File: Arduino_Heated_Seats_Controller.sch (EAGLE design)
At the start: 21 parts, among them U1 MEGA8-AI, U2 UA78M05CDCY, U3 ULN2003ADE4, U4 IC_TD62783-SO-18W

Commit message: Library error - need to make sure the rest of my libraries are correct are well.
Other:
- moved on the sheet: U4

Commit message: More patching.
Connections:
- net VIN: now also U3.COM
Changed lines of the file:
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@@
 <instance part="SUPPLY16" gate="GND" x="116.84" y="99.06"/>
 <instance part="SUPPLY12" gate="GND" x="154.94" y="109.22"/>
-<instance part="SUPPLY17" gate="GND" x="132.08" y="63.754"/>
+<instance part="SUPPLY17" gate="GND" x="129.54" y="63.754"/>
 <instance part="R1" gate="G$1" x="157.48" y="132.08"/>
 <instance part="R2" gate="G$1" x="167.64" y="134.62"/>
@@
 <segment>
 <pinref part="SUPPLY17" gate="GND" pin="GND"/>
-<wire x1="132.08" y1="66.294" x2="132.08" y2="68.58" width="0.1524" layer="91"/>
+<wire x1="129.54" y1="66.294" x2="129.54" y2="66.04" width="0.1524" layer="91"/>
 <pinref part="U3" gate="A" pin="E"/>
-<wire x1="139.7" y1="71.12" x2="132.08" y2="71.12" width="0.1524" layer="91"/>
-<wire x1="132.08" y1="68.58" x2="132.08" y2="71.12" width="0.1524" layer="91"/>
+<wire x1="139.7" y1="71.12" x2="129.54" y2="71.12" width="0.1524" layer="91"/>
+<wire x1="129.54" y1="66.04" x2="129.54" y2="71.12" width="0.1524" layer="91"/>
 </segment>
 </net>
@@
 <junction x="33.02" y="139.7"/>
 </segment>
+<segment>
+<pinref part="U3" gate="A" pin="COM"/>
+<wire x1="137.16" y1="68.58" x2="139.7" y2="68.58" width="0.1524" layer="91"/>
+<wire x1="137.16" y1="68.58" x2="135.89" y2="68.58" width="0.1524" layer="91"/>
+<label x="135.89" y="68.58" size="1.27" layer="95" rot="R180" xref="yes"/>
+</segment>
 </net>

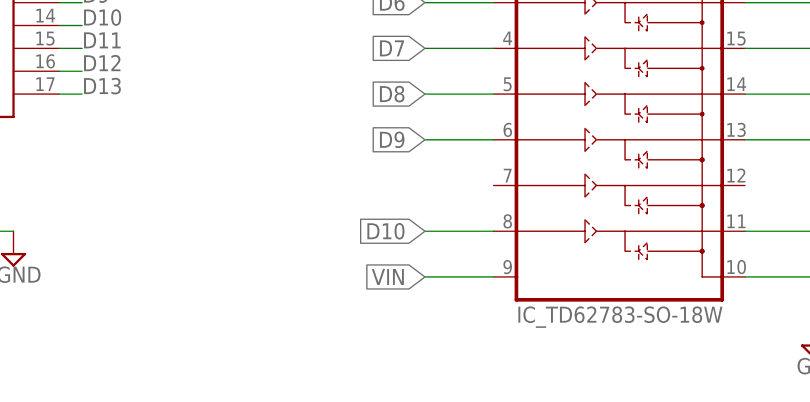
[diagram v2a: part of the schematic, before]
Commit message: Grounding unused input pins (compatibility with A2982SLWTR-T). Tweak routing and vias.
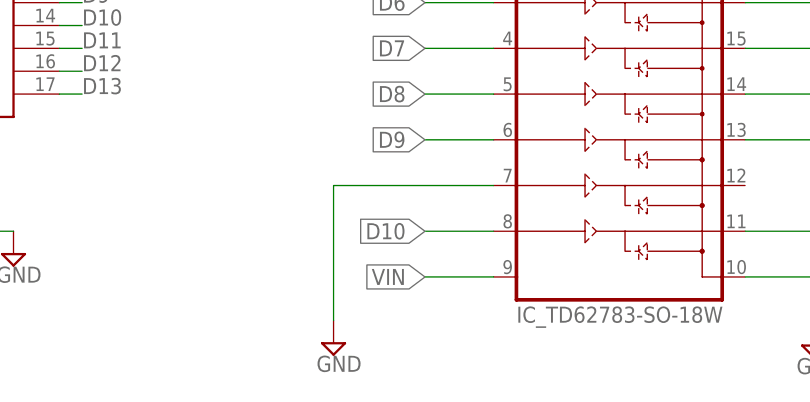
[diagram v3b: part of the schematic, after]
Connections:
- net GND: now also U4.IN7
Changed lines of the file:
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@@
 <part name="SUPPLY9" library="supply2" deviceset="GND" device=""/>
 <part name="C2" library="rcl" deviceset="C-US" device="C0603" value="0.1uF"/>
+<part name="SUPPLY13" library="supply2" deviceset="GND" device=""/>
 </parts>
 <sheets>
@@
 <instance part="SUPPLY9" gate="GND" x="78.74" y="104.14"/>
 <instance part="C2" gate="G$1" x="27.94" y="119.38"/>
+<instance part="SUPPLY13" gate="GND" x="124.46" y="2.794"/>
 </instances>
 <busses>
@@
 <wire x1="129.54" y1="66.04" x2="129.54" y2="71.12" width="0.1524" layer="91"/>
 </segment>
+<segment>
+<pinref part="U4" gate="IC" pin="IN7"/>
+<wire x1="142.24" y1="20.32" x2="124.46" y2="20.32" width="0.1524" layer="91"/>
+<wire x1="124.46" y1="20.32" x2="124.46" y2="5.334" width="0.1524" layer="91"/>
+<pinref part="SUPPLY13" gate="GND" pin="GND"/>
+</segment>
 </net>

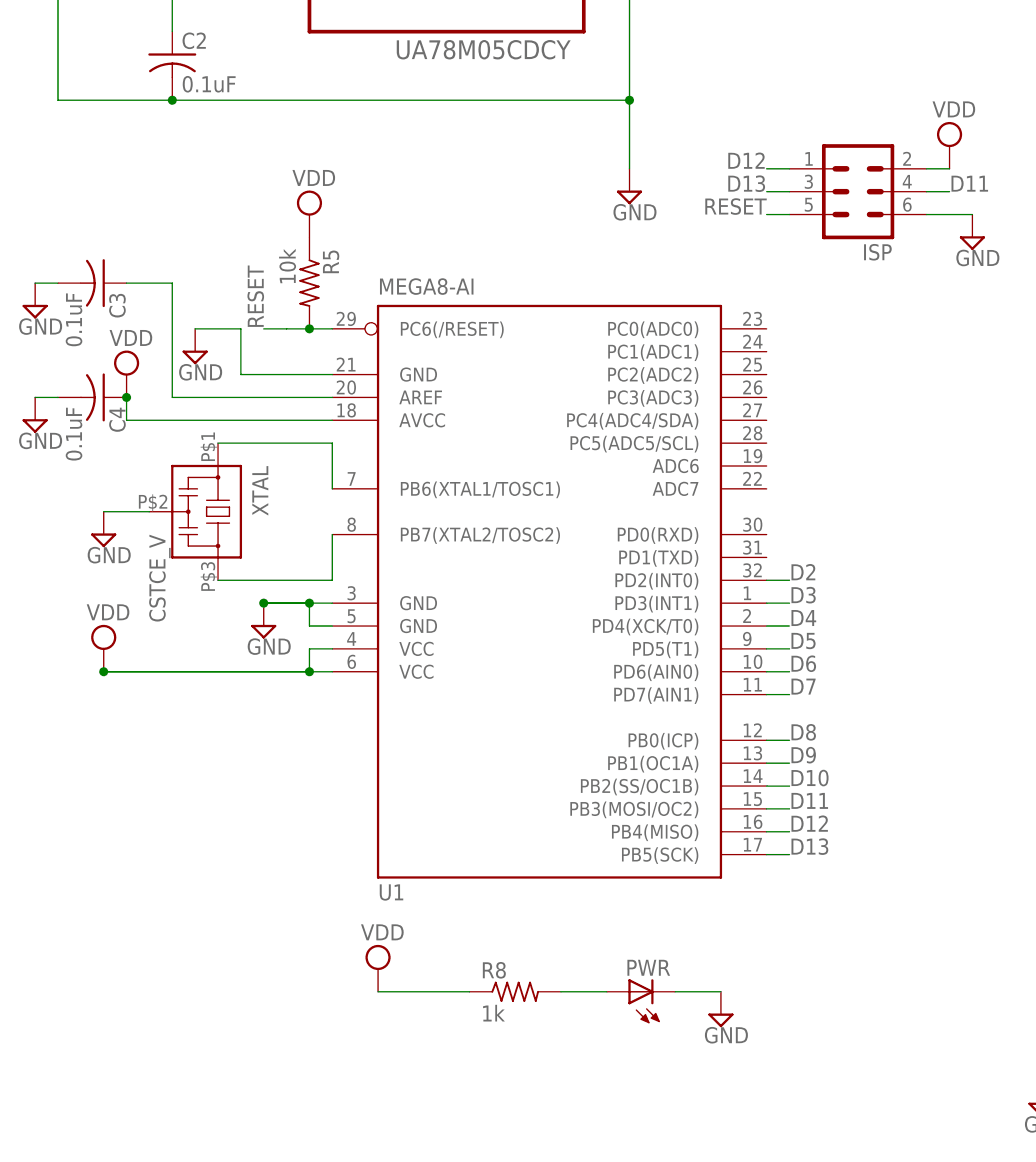
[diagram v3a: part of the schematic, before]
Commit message: Swapped ATMega from unknown library with Element14 library. Moved silkscreen (web address) to other side of board.
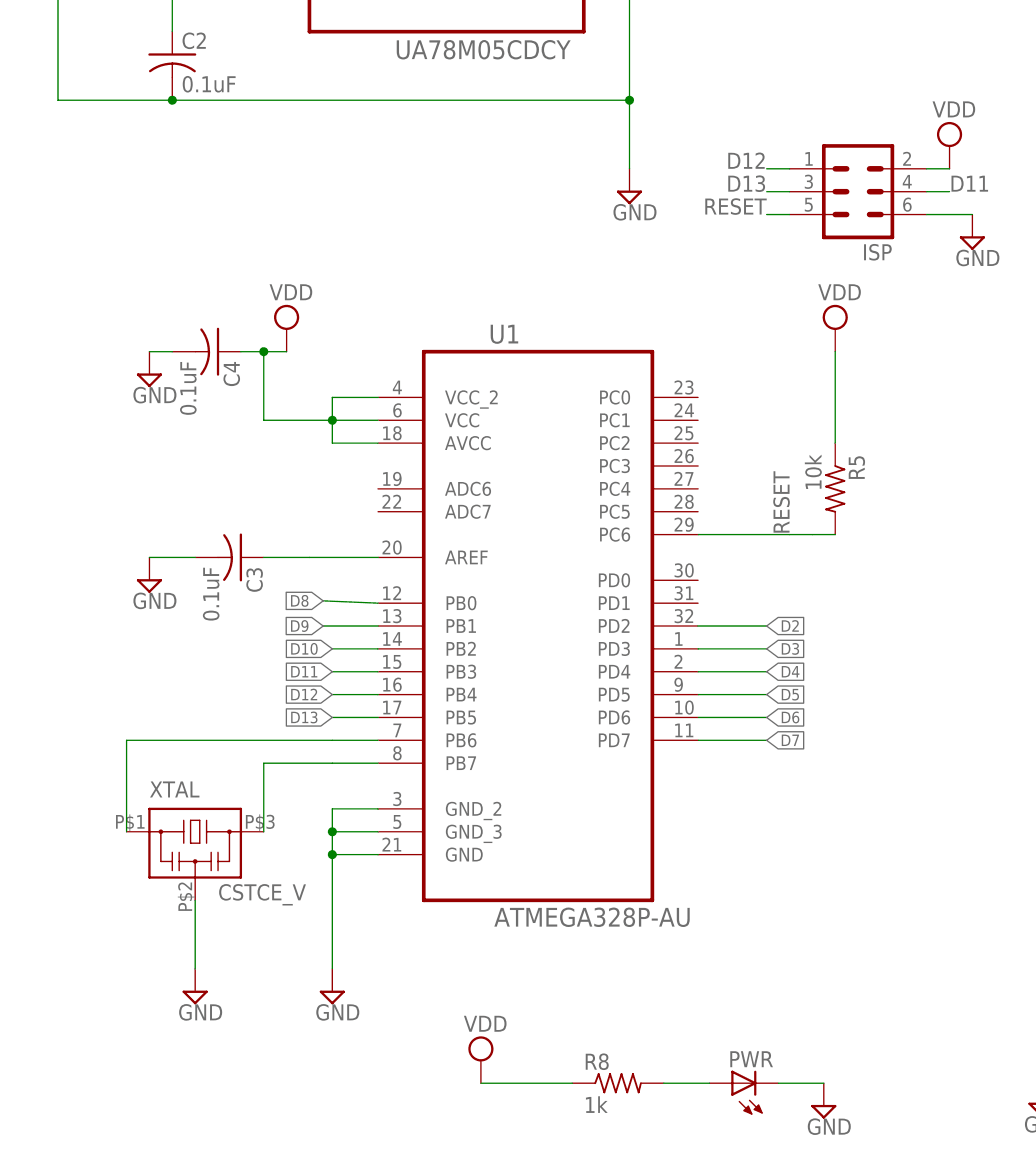
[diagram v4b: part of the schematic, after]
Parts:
- U1: value MEGA8-AI -> ATMEGA328P-AU; device atmel:MEGA8-AI -> Atmel_By_element14_Batch_1-00:ATMEGA328P-AU
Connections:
- net D10: now also U1.PB2; no longer U1.PB2(SS/OC1B)
- net D11: now also U1.PB3; no longer U1.PB3(MOSI/OC2)
- net D12: now also U1.PB4; no longer U1.PB4(MISO)
- net D13: now also U1.PB5; no longer U1.PB5(SCK)
- net D2: now also U1.PD2; no longer U1.PD2(INT0)
- net D3: now also U1.PD3; no longer U1.PD3(INT1)
- net D4: now also U1.PD4; no longer U1.PD4(XCK/T0)
- net D5: now also U1.PD5; no longer U1.PD5(T1)
- net D6: now also U1.PD6; no longer U1.PD6(AIN0)
- net D7: now also U1.PD7; no longer U1.PD7(AIN1)
- net D8: now also U1.PB0; no longer U1.PB0(ICP)
- net D9: now also U1.PB1; no longer U1.PB1(OC1A)
- net GND: now also U1.GND_2, U1.GND_3; no longer U1.GND@1, U1.GND@2
- net PB6: now also U1.PB6; no longer U1.PB6(XTAL1/TOSC1)
- net PB7: now also U1.PB7; no longer U1.PB7(XTAL2/TOSC2)
- net RESET: now also U1.PC6; no longer U1.PC6(/RESET)
- net VDD: now also U1.VCC, U1.VCC_2; no longer U1.VCC@1, U1.VCC@2
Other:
- moved on the sheet: C3, C4, PWR, R5, R8, XTAL

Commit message: Enough changes to warrant a minor revision bump. Equivalent parts have been selected for testing - will need to update design if tests are good. Current design should be compatible with selected parts (will order parts before sending to fab house).
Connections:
- net D-BTN: now also BTN-IN.2, R2.1; no longer BTN-IN.1, R1.1
- net D2: now also R2.2, R4.1; no longer R1.2, R3.1
- net D3: now also R1.2, R3.1; no longer R2.2, R4.1
- net P-BTN: now also BTN-IN.1, R1.1; no longer BTN-IN.2, R2.1
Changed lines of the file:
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@@
 <net name="D2" class="0">
+<segment>
+<pinref part="U1" gate="A" pin="PD2"/>
+<wire x1="86.36" y1="55.88" x2="93.98" y2="55.88" width="0.1524" layer="91"/>
+<label x="93.98" y="55.88" size="1.27" layer="95" xref="yes"/>
+</segment>
+<segment>
+<wire x1="180.34" y1="121.92" x2="180.34" y2="134.62" width="0.1524" layer="91"/>
+<wire x1="180.34" y1="134.62" x2="172.72" y2="134.62" width="0.1524" layer="91"/>
+<wire x1="180.34" y1="134.62" x2="187.96" y2="134.62" width="0.1524" layer="91"/>
+<junction x="180.34" y="134.62"/>
+<label x="187.96" y="134.62" size="1.27" layer="95" xref="yes"/>
+<pinref part="R2" gate="G$1" pin="2"/>
+<pinref part="R4" gate="G$1" pin="1"/>
+</segment>
+</net>
+<net name="D3" class="0">
+<segment>
+<pinref part="U1" gate="A" pin="PD3"/>
+<wire x1="86.36" y1="53.34" x2="93.98" y2="53.34" width="0.1524" layer="91"/>
+<label x="93.98" y="53.34" size="1.27" layer="95" xref="yes"/>
+</segment>
 <segment>
 <wire x1="175.26" y1="129.54" x2="175.26" y2="132.08" width="0.1524" layer="91"/>
@@
 <pinref part="R3" gate="G$1" pin="1"/>
 </segment>
-<segment>
-<pinref part="U1" gate="A" pin="PD2"/>
-<wire x1="86.36" y1="55.88" x2="93.98" y2="55.88" width="0.1524" layer="91"/>
-<label x="93.98" y="55.88" size="1.27" layer="95" xref="yes"/>
-</segment>
-</net>
-<net name="D3" class="0">
-<segment>
-<wire x1="180.34" y1="121.92" x2="180.34" y2="134.62" width="0.1524" layer="91"/>
-<wire x1="180.34" y1="134.62" x2="172.72" y2="134.62" width="0.1524" layer="91"/>
-<wire x1="180.34" y1="134.62" x2="187.96" y2="134.62" width="0.1524" layer="91"/>
-<junction x="180.34" y="134.62"/>
-<label x="187.96" y="134.62" size="1.27" layer="95" xref="yes"/>
-<pinref part="R2" gate="G$1" pin="2"/>
-<pinref part="R4" gate="G$1" pin="1"/>
-</segment>
-<segment>
-<pinref part="U1" gate="A" pin="PD3"/>
-<wire x1="86.36" y1="53.34" x2="93.98" y2="53.34" width="0.1524" layer="91"/>
-<label x="93.98" y="53.34" size="1.27" layer="95" xref="yes"/>
-</segment>
 </net>
 <net name="D-BTN" class="0">
-<segment>
-<wire x1="152.4" y1="132.08" x2="139.7" y2="132.08" width="0.1524" layer="91"/>
-<pinref part="BTN-IN" gate="G$1" pin="1"/>
-<label x="144.78" y="132.08" size="1.27" layer="95" rot="R270" xref="yes"/>
-<pinref part="R1" gate="G$1" pin="1"/>
-</segment>
-</net>
-<net name="P-BTN" class="0">
 <segment>
 <pinref part="BTN-IN" gate="G$1" pin="2"/>
@@
 </segment>
 </net>
+<net name="P-BTN" class="0">
+<segment>
+<wire x1="152.4" y1="132.08" x2="139.7" y2="132.08" width="0.1524" layer="91"/>
+<pinref part="BTN-IN" gate="G$1" pin="1"/>
+<label x="144.78" y="132.08" size="1.27" layer="95" rot="R270" xref="yes"/>
+<pinref part="R1" gate="G$1" pin="1"/>
+</segment>
+</net>

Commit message: Changes from freelancer.com - lovely~
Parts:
- removed PWR: (no value), led:LEDCHIP-LED0603
- removed R8: 1k, resistor:R-US_R0603
- added L, ON: (no value), led:LEDCHIP-LED0603
- added R6, R7: 1K, resistor:R-US_R0603
- R1, R2: value 15k -> 15K
- R3, R4, R5: value 10k -> 10K
- U2: value UA78M05CDCY -> UA78M05; device Texas Instruments_By_element14_Batch_1:UA78M05CDCY -> Roylib Regulator:UA78M05
- U3: value ULN2003ADE4 -> TPL7407L; device Texas Instruments_By_element14_Batch_1:ULN2003ADE4 -> Roylib Drivers:TPL7407L
- U4: value IC_TD62783-SO-18W -> A2982; device dp_devices:IC_TD62783-SO-18W -> Roylib Drivers:A2982
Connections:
- new net N$1: L.A, R6.2
- net D13: now also R6.1
- net D4: now also U3.IN7; no longer U3.7B
- net D5: now also U3.IN6; no longer U3.6B
- net D6: now also U3.IN5; no longer U3.5B
- net D7: now also U3.IN3; no longer U3.3B
- net D8: now also U3.IN2; no longer U3.2B
- net D9: now also U3.IN1; no longer U3.1B
- net DL-HIGH: now also U3.!OUT7; no longer U3.7C
- net DL-LOW: now also U3.!OUT5; no longer U3.5C
- net DL-MID: now also U3.!OUT6; no longer U3.6C
- net GND: now also L.C, ON.C, U2.GND, U3.GND; no longer PWR.C, U2.COMMON, U2.COMMON_2, U3.E
- net N$3: now also ON.A, R7.2; no longer PWR.A, R8.2
- net PL-HIGH: now also U3.!OUT3; no longer U3.3C
- net PL-LOW: now also U3.!OUT1; no longer U3.1C
- net PL-MID: now also U3.!OUT2; no longer U3.2C
- net VDD: now also R7.1, U2.OUT; no longer R8.1, U2.OUTPUT
- net VIN: now also U2.IN, U4.+VS; no longer U2.INPUT, U4.VS
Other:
- moved on the sheet: BTN-IN, C1, C2, C3, C4, H-OUT, ISP, LED-OUT, PWR/H, R1, R2, R3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
